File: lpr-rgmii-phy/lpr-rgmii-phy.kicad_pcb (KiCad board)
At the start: 4 copper layers, 0 parts

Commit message: lpr-rgmii-phy: Finished initial layout, ready for review
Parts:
- added C1: 22 uF, azonenberg_pcb:EIA_1812_CAP_NOSILK, F.Cu at (76.2, 109.2)
- added C10: 4.7 uF, azonenberg_pcb:EIA_0603_CAP_NOSILK, F.Cu at (54.0, 84.2)
- added C11: 4.7 uF, azonenberg_pcb:EIA_0603_CAP_NOSILK, F.Cu at (68.5, 101.5)
- added C12: 4.7 uF, azonenberg_pcb:EIA_0603_CAP_NOSILK, F.Cu at (57.5, 82.0)
- added C13: 0.1 uF, azonenberg_pcb:EIA_0402_CAP_NOSILK, B.Cu at (54.5, 109.8)
- added C14: 0.1 uF, azonenberg_pcb:EIA_0402_CAP_NOSILK, B.Cu at (55.8, 112.2)
- added C15: 0.1 uF, azonenberg_pcb:EIA_0402_CAP_NOSILK, B.Cu at (69.5, 112.2)
- added C16: 0.1 uF, azonenberg_pcb:EIA_0402_CAP_NOSILK, B.Cu at (70.5, 109.8)
- added C17: 0.47 uF, azonenberg_pcb:EIA_0402_CAP_NOSILK, B.Cu at (61.2, 85.1)
- added C18: 0.47 uF, azonenberg_pcb:EIA_0402_CAP_NOSILK, B.Cu at (62.6, 85.5)
- added C19: 4.7 uF, azonenberg_pcb:EIA_0603_CAP_NOSILK, F.Cu at (54.0, 78.0)
- added C2: 22 uF, azonenberg_pcb:EIA_1210_CAP_NOSILK, F.Cu at (74.8, 117.2)
- added C20: 4.7 uF, azonenberg_pcb:EIA_0603_CAP_NOSILK, F.Cu at (58.6, 93.8)
- added C21: 4.7 uF, azonenberg_pcb:EIA_0603_CAP_NOSILK, F.Cu at (68.5, 97.5)
- added C22: 4.7 uF, azonenberg_pcb:EIA_0603_CAP_NOSILK, F.Cu at (57.5, 97.8)
- added C23: 0.47 uF, azonenberg_pcb:EIA_0402_CAP_NOSILK, B.Cu at (64.5, 88.7)
- added C24: 0.47 uF, azonenberg_pcb:EIA_0402_CAP_NOSILK, B.Cu at (64.0, 84.9)
- added C25: 0.47 uF, azonenberg_pcb:EIA_0402_CAP_NOSILK, B.Cu at (63.4, 90.9)
- added C26: 0.47 uF, azonenberg_pcb:EIA_0402_CAP_NOSILK, B.Cu at (60.1, 88.7)
- added C27: 0.47 uF, azonenberg_pcb:EIA_0402_CAP_NOSILK, B.Cu at (59.2, 91.8)
- added C28: 0.47 uF, azonenberg_pcb:EIA_0402_CAP_NOSILK, B.Cu at (60.0, 86.6)
- added C29: 0.47 uF, azonenberg_pcb:EIA_0402_CAP_NOSILK, B.Cu at (65.0, 85.7)
- added C3: 22 uF, azonenberg_pcb:EIA_1210_CAP_NOSILK, F.Cu at (78.2, 117.2)
- added C30: 0.47 uF, azonenberg_pcb:EIA_0402_CAP_NOSILK, B.Cu at (59.1, 90.2)
- added C31: 0.47 uF, azonenberg_pcb:EIA_0402_CAP_NOSILK, B.Cu at (60.9, 90.8)
- added C32: 0.47 uF, azonenberg_pcb:EIA_0402_CAP_NOSILK, B.Cu at (64.5, 87.6)
- added C33: 0.47 uF, azonenberg_pcb:EIA_0402_CAP_NOSILK, B.Cu at (65.8, 91.8)
- added C34: 0.47 uF, azonenberg_pcb:EIA_0402_CAP_NOSILK, B.Cu at (64.6, 89.6)
- added C35: 0.47 uF, azonenberg_pcb:EIA_0402_CAP_NOSILK, B.Cu at (57.8, 85.7)
- added C4: 22 uF, azonenberg_pcb:EIA_1812_CAP_NOSILK, F.Cu at (76.5, 122.5)
- added C5: 22 uF, azonenberg_pcb:EIA_1210_CAP_NOSILK, F.Cu at (78.0, 130.0)
- added C6: 22 uF, azonenberg_pcb:EIA_1210_CAP_NOSILK, F.Cu at (74.0, 130.0)
- added C7: 0.47 uF, azonenberg_pcb:EIA_0402_CAP_NOSILK, F.Cu at (55.1, 90.9)
- added C8: 4.7 uF, azonenberg_pcb:EIA_0603_CAP_NOSILK, F.Cu at (54.0, 82.0)
- added C9: 4.7 uF, azonenberg_pcb:EIA_0603_CAP_NOSILK, F.Cu at (55.0, 93.8)
- added FB1: MI0603J601R-10, azonenberg_pcb:EIA_0603_INDUCTOR_NOSILK, F.Cu at (53.2, 80.0)
- added FB2: MI0603J601R-10, azonenberg_pcb:EIA_0603_INDUCTOR_NOSILK, F.Cu at (56.8, 93.0)
- added FB3: MI0603J601R-10, azonenberg_pcb:EIA_0603_INDUCTOR_NOSILK, F.Cu at (67.8, 99.5)
- added FB4: MI0603J601R-10, azonenberg_pcb:EIA_0603_INDUCTOR_NOSILK, F.Cu at (55.5, 98.5)
- added J1: LPR_HEADER, azonenberg_pcb:CONN_HEADER_2.0MM_2x20_SMT_MOLEX_0877594014, B.Cu at (77.4, 81.5)
- added J2: 0826-1G1T-23-F, azonenberg_pcb:CONN_BELFUSE_0826_1G1T_23_F, F.Cu at (62.5, 127.5)
- added M1: LOGO, azonenberg_pcb:LONGTHING-1200DPI, F.Cu at (78.5, 64.9)
- added M2: LOGO, w_logo:Logo_silk_OSHW_6x6mm, F.Cu at (77.5, 79.0)
- added M3: LOGO, w_logo:Logo_silk_ROHS_5x2.8mm, F.Cu at (77.5, 84.0)
- added M4: LOGO, w_logo:Logo_silk_WEEE_3.4x5mm, F.Cu at (77.5, 73.0)
- added R1: 100K, azonenberg_pcb:EIA_0402_RES_NOSILK, F.Cu at (79.0, 114.2)
- added R10: 33, azonenberg_pcb:EIA_0402_RES_NOSILK, F.Cu at (63.8, 79.5)
- added R11: 33, azonenberg_pcb:EIA_0402_RES_NOSILK, F.Cu at (62.2, 81.5)
- added R12: 33, azonenberg_pcb:EIA_0402_RES_NOSILK, F.Cu at (61.8, 79.5)
- added R13: 33, azonenberg_pcb:EIA_0402_RES_NOSILK, F.Cu at (61.2, 81.5)
- added R14: 33, azonenberg_pcb:EIA_0402_RES_NOSILK, F.Cu at (60.2, 81.5)
- added R15: 12.1K 1%, azonenberg_pcb:EIA_0402_RES_NOSILK, F.Cu at (57.6, 90.2)
- added R16: 1K, azonenberg_pcb:EIA_0402_RES_NOSILK, B.Cu at (67.7, 105.3)
- added R17: 10K, azonenberg_pcb:EIA_0402_RES_NOSILK, F.Cu at (57.8, 86.8)
- added R18: 10K, azonenberg_pcb:EIA_0402_RES_NOSILK, B.Cu at (64.2, 81.5)
- added R19: 10K, azonenberg_pcb:EIA_0402_RES_NOSILK, B.Cu at (63.8, 79.5)
- added R2: 22.1K, azonenberg_pcb:EIA_0402_RES_NOSILK, F.Cu at (80.0, 114.3)
- added R20: 10K, azonenberg_pcb:EIA_0402_RES_NOSILK, B.Cu at (62.2, 81.5)
- added R21: 10K, azonenberg_pcb:EIA_0402_RES_NOSILK, B.Cu at (61.8, 79.5)
- added R22: 10K, azonenberg_pcb:EIA_0402_RES_NOSILK, B.Cu at (61.2, 81.5)
- added R23: 10K, azonenberg_pcb:EIA_0402_RES_NOSILK, B.Cu at (60.2, 81.5)
- added R24: 1K, azonenberg_pcb:EIA_0402_RES_NOSILK, B.Cu at (58.2, 84.2)
- added R25: 10K, azonenberg_pcb:EIA_0402_RES_NOSILK, F.Cu at (79.5, 113.0)
- added R26: 10K, azonenberg_pcb:EIA_0402_RES_NOSILK, F.Cu at (79.0, 125.5)
- added R3: 100K, azonenberg_pcb:EIA_0402_RES_NOSILK, F.Cu at (78.7, 126.9)
- added R4: 100K, azonenberg_pcb:EIA_0402_RES_NOSILK, F.Cu at (80.2, 126.4)
- added R5: 470, azonenberg_pcb:EIA_0402_RES_NOSILK, B.Cu at (66.0, 105.2)
- added R6: 470, azonenberg_pcb:EIA_0402_RES_NOSILK, B.Cu at (56.5, 105.2)
- added R7: 33, azonenberg_pcb:EIA_0402_RES_NOSILK, F.Cu at (57.0, 89.2)
- added R8: 1K, azonenberg_pcb:EIA_0402_RES_NOSILK, B.Cu at (58.9, 105.3)
- added R9: 33, azonenberg_pcb:EIA_0402_RES_NOSILK, F.Cu at (64.2, 81.5)
- added TP1: U.FL, azonenberg_pcb:CONN_U.FL_TE_1909763-1, F.Cu at (52.2, 63.0)
- added TP2: U.FL, azonenberg_pcb:CONN_U.FL_TE_1909763-1, F.Cu at (80.8, 90.8)
- added TP3: U.FL, azonenberg_pcb:CONN_U.FL_TE_1909763-1, F.Cu at (51.8, 74.0)
- added TP4: U.FL, azonenberg_pcb:CONN_U.FL_TE_1909763-1, F.Cu at (51.8, 87.7)
- added TP5: U.FL, azonenberg_pcb:CONN_U.FL_TE_1909763-1, F.Cu at (70.0, 94.0)
- added TP6: U.FL, azonenberg_pcb:CONN_U.FL_TE_1909763-1, F.Cu at (51.8, 93.8)
- added TP7: TESTPOINT, azonenberg_pcb:TESTPOINT_SMT_0.5MM, F.Cu at (78.5, 124.8)
- added TP8: TESTCLIP, azonenberg_pcb:TESTPOINT_SMT_KEYSTONE_5016, F.Cu at (77.5, 105.0)
- added TP9: TESTPOINT, azonenberg_pcb:TESTPOINT_SMT_0.5MM, F.Cu at (79.0, 112.2)
- added U1: MUN12AD03-SE, azonenberg_pcb:MODULE_CYNTEC_MUN12AD03-SE, F.Cu at (76.5, 113.2)
- added U2: MUN12AD03-SE, azonenberg_pcb:MODULE_CYNTEC_MUN12AD03-SE, F.Cu at (76.5, 126.0)
- added U3: ECS-1612MV-250-CN, azonenberg_pcb:OSCILLATOR_1.6x1.2, F.Cu at (55.1, 89.6)
- added U4: KSZ9031RN, azonenberg_pcb:QFN_48_0.5MM_7x7MM, F.Cu at (62.5, 87.5)
- added U5: RCLAMP0514M, azonenberg_pcb:SOP_10_0.5MM_3MM, F.Cu at (60.5, 99.5)
- added U6: RCLAMP0514M, azonenberg_pcb:SOP_10_0.5MM_3MM, F.Cu at (64.2, 99.5)
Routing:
- net /GND: track 0.00 -> 459.7 mm, vias 0 -> 221
- net /3V3: track 0.00 -> 152.4 mm, vias 0 -> 30
- net /1V2: track 0.00 -> 106.4 mm, vias 0 -> 24
- net /5V5: track 0.00 -> 66.6 mm, vias 0 -> 26
- net /D1V2: track 0.00 -> 51.0 mm, vias 0 -> 10
- net /ETH_RX_CLK: track 0.00 -> 32.7 mm, vias 0 -> 1
- net /A3V3: track 0.00 -> 31.0 mm, vias 0 -> 7
- net /ETH_RXD0: track 0.00 -> 27.1 mm, vias 0 -> 1
- net /ETH_RX_DV: track 0.00 -> 25.9 mm, vias 0 -> 1
- net /ETH_LED2_N: track 0.00 -> 25.8 mm, vias 0 -> 1
- net /ETH_LED1_N: track 0.00 -> 23.3 mm
- net /ETH_B_P: track 0.00 -> 22.8 mm
- net /ETH_RXD2: track 0.00 -> 22.8 mm, vias 0 -> 1
- net /ETH_B_N: track 0.00 -> 22.7 mm
- net /ETH_RXD1: track 0.00 -> 22.6 mm, vias 0 -> 1
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- added copper zone on B.Cu, net /1V2
- added copper zone on F.Cu, net /1V2
- added copper zone on In2.Cu, net /1V2
- added copper zone on F.Cu, net /3V3
- added copper zone on In2.Cu, net /3V3
- added copper zone on B.Cu, net /5V5
- added copper zone on F.Cu, net /5V5
- added copper zone on In2.Cu, net /5V5
- added copper zone on In2.Cu, net /A1V2
- added copper zone on In2.Cu, net /A3V3
- added copper zone on In2.Cu, net /D1V2
- added copper zone on F.Cu, net /GND
- added copper zone on In1.Cu, net /GND
- added copper zone on In2.Cu, net /GND
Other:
- board outline added: 35 x 73.5 mm
- board text added: "1V2"
- board text added: "3V3"
- board text added: "A1V2"
- board text added: "A1V2 _PLL"
- board text added: "A3V3"
- board text added: "D1V2"
- board text added: "GND"
- board text added: "KU+ HDIO RGMII Test for LPR RRH A. Zonenberg 2024-07-07 v0.1"

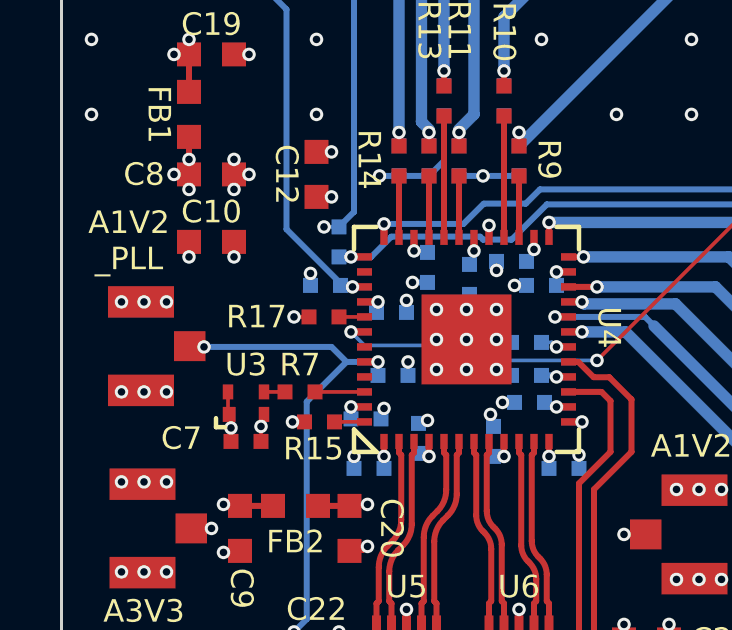
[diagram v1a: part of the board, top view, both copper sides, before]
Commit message: Minor changes to layout made during design review
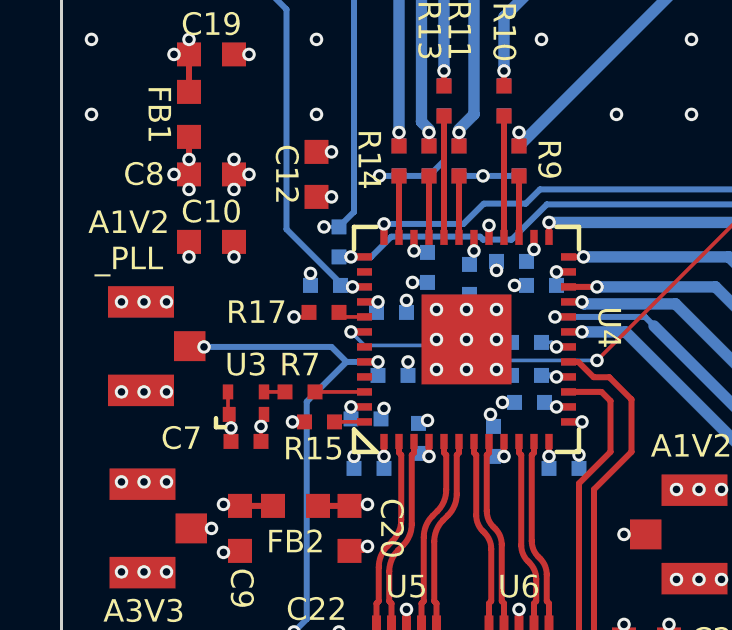
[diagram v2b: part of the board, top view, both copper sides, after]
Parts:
- moved R17 0.15 mm to (57.8, 86.6)
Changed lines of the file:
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@@
 			(usegerberattributes yes)
 			(usegerberadvancedattributes yes)
-			(creategerberjobfile yes)
+			(creategerberjobfile no)
 			(dashed_line_dash_ratio 12.000000)
 			(dashed_line_gap_ratio 3.000000)
@@
 			(outputformat 1)
 			(mirror no)
-			(drillshape 1)
+			(drillshape 0)
 			(scaleselection 1)
-			(outputdirectory "")
+			(outputdirectory "output/")
 		)
 	)
@@
 	(footprint "azonenberg_pcb:EIA_0402_RES_NOSILK"
 		(layer "F.Cu")
-		(at 57.75 86.75)
+		(at 57.75 86.6)
 		(property "Reference" "R17"
 			(at -2.25 0 0)
@@
 		(at 62.6 85.5 -90)
 		(property "Reference" "C18"
-			(at -2.3 0 90)
+			(at -2 0.4 90)
 			(unlocked yes)
 			(layer "B.SilkS")

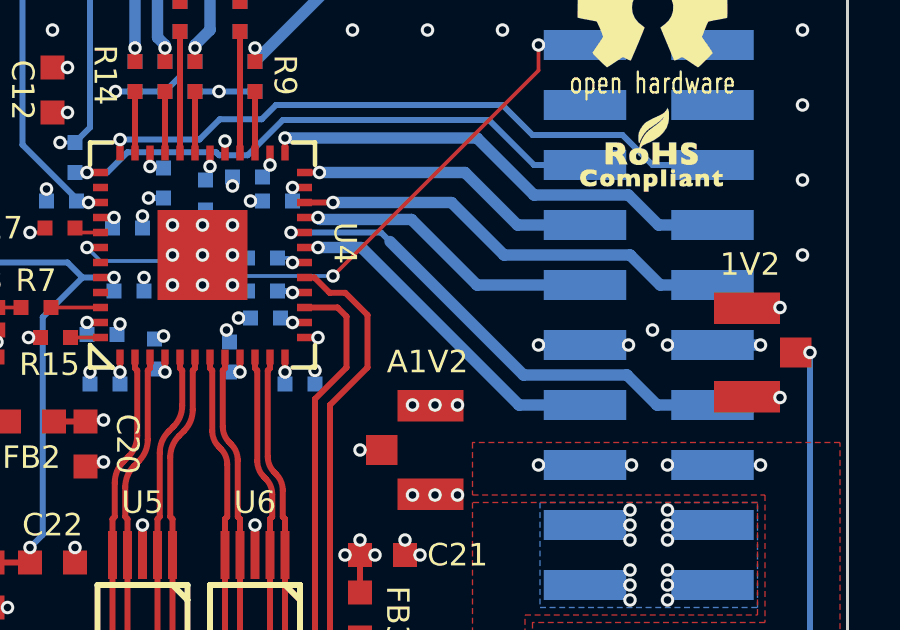
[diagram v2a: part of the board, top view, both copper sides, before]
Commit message: Added additioanl stitching vias
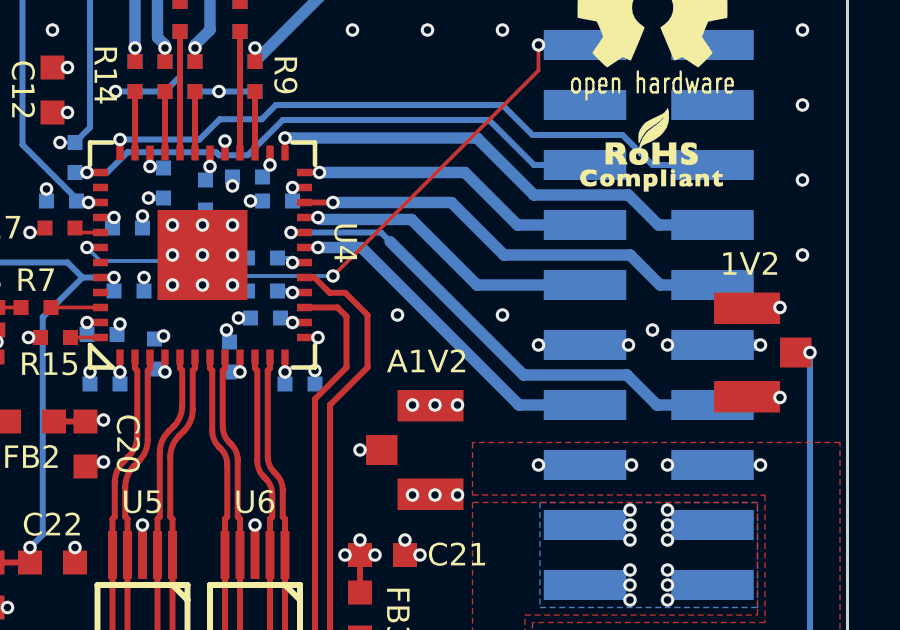
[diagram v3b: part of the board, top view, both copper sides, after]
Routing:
- net /GND: vias 221 -> 223
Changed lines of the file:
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@@
+	)
+	(via
+		(at 69 89.5)
+		(size 0.45)
+		(drill 0.25)
+		(layers "F.Cu" "B.Cu")
+		(net 1)
 	)
 	(via
@@
 		(size 0.45)
 		(drill 0.25)
+		(layers "F.Cu" "B.Cu")
+		(net 1)
+	)
+	(via
+		(at 72.5 89.5)
+		(size 0.45)
+		(drill 0.25)
